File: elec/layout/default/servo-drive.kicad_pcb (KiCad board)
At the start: 4 copper layers, 37.6 x 39.9 mm, 125 parts

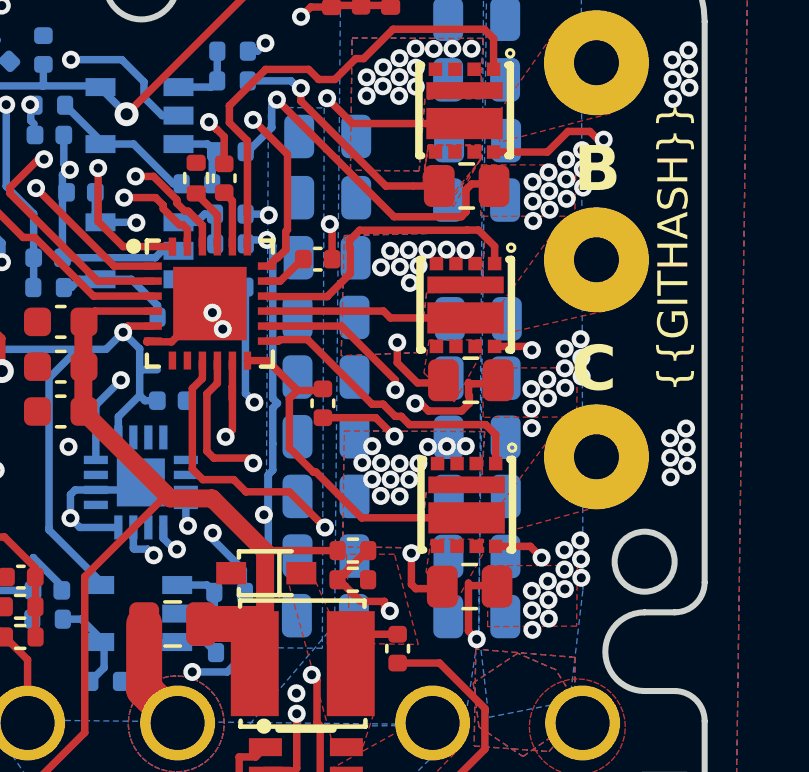
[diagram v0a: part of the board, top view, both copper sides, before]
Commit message: Flip net-ties to match improved flow
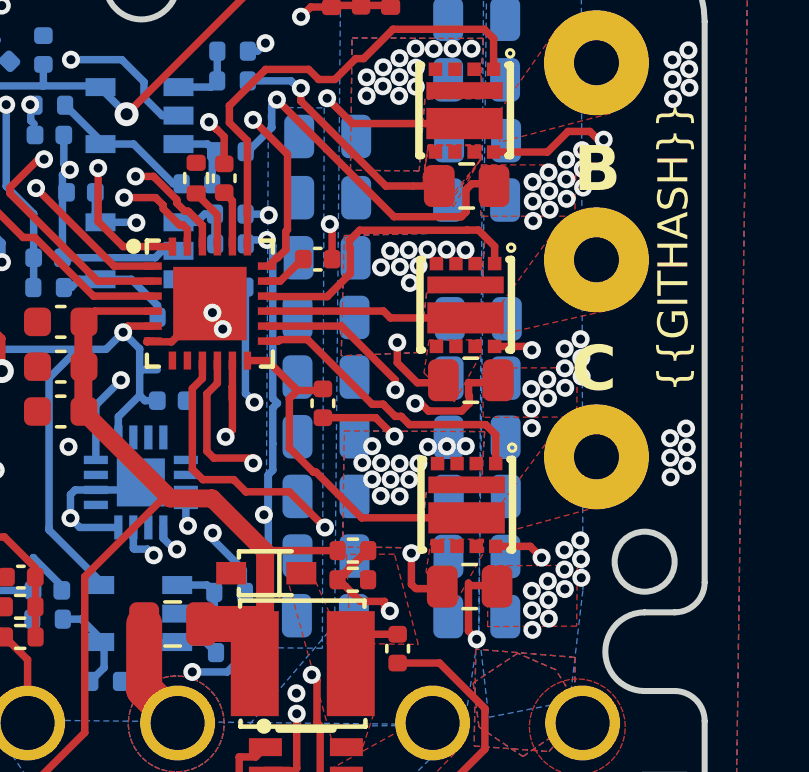
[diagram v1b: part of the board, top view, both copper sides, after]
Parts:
- C24: value 16V 220nF X7R ±10% 0402 Multilayer Ceramic Capacitors MLCC - SMD/SMT ROHS -> 16V 100nF X7R ±10% 0402 Multilayer Ceramic Capacitors MLCC - SMD/SMT ROHS
- C42, C44: value 50V 20pF C0G ±5% 0402 Multilayer Ceramic Capacitors MLCC - SMD/SMT ROHS -> 50V 18pF C0G ±5% 0402 Multilayer Ceramic Capacitors MLCC - SMD/SMT ROHS
- C9: value 50V 1uF X5R ±10% 0603 Multilayer Ceramic Capacitors MLCC - SMD/SMT ROHS -> 10V 10uF X5R ±10% 0603 Multilayer Ceramic Capacitors MLCC - SMD/SMT ROHS
- R1, R15, R20, R38: value 62.5mW Thick Film Resistors ±100ppm/℃ ±1% 10kΩ 0402 Chip Resistor - Surface Mount ROHS -> 62.5mW Thick Film Resistors 50V ±100ppm/℃ ±1% 10kΩ 0402 Chip Resistor - Surface Mount ROHS
- R10: value 62.5mW Thick Film Resistors ±100ppm/℃ ±1% 27.4kΩ 0402 Chip Resistor - Surface Mount ROHS -> 62.5mW Thick Film Resistors 50V ±100ppm/℃ ±1% 27.4kΩ 0402 Chip Resistor - Surface Mount ROHS
- R11: value 62.5mW ±1% ±200ppm/℃ 3.01kΩ 0402 Chip Resistor - Surface Mount ROHS -> 62.5mW Thick Film Resistors 50V ±100ppm/℃ ±1% 3kΩ 0402 Chip Resistor - Surface Mount ROHS
- R12, R14, R26, R45, R49, R51: value 62.5mW Thick Film Resistors ±100ppm/℃ ±1% 47kΩ 0402 Chip Resistor - Surface Mount ROHS -> 62.5mW Thick Film Resistors 50V ±100ppm/℃ ±1% 47kΩ 0402 Chip Resistor - Surface Mount ROHS
- R13, R2, R25, R44, R48, R50, R6: value 62.5mW Thick Film Resistors ±100ppm/℃ ±1% 1kΩ 0402 Chip Resistor - Surface Mount ROHS -> 62.5mW Thick Film Resistors 50V ±100ppm/℃ ±1% 1kΩ 0402 Chip Resistor - Surface Mount ROHS
- R16, R46, R52: value 62.5mW ±1% ±200ppm/℃ 73.2Ω 0402 Chip Resistor - Surface Mount ROHS -> 62.5mW Thick Film Resistors 50V -200ppm/℃~+500ppm/℃ ±1% 6.04Ω 0402 Chip Resistor - Surface Mount ROHS
- R17: value 62.5mW Thick Film Resistors ±100ppm/℃ ±1% 20.5kΩ 0402 Chip Resistor - Surface Mount ROHS -> 62.5mW Thick Film Resistors 50V ±100ppm/℃ ±1% 20.5kΩ 0402 Chip Resistor - Surface Mount ROHS
- R18: value 62.5mW Thick Film Resistors ±100ppm/℃ ±1% 6.34kΩ 0402 Chip Resistor - Surface Mount ROHS -> 62.5mW Thick Film Resistors 50V ±100ppm/℃ ±1% 6.34kΩ 0402 Chip Resistor - Surface Mount ROHS
- R19: value 10 +/- 0.1 (1%) kiloohm -> 10kohm +/- 1%
- R21: value 62.5mW Thick Film Resistors ±100ppm/℃ ±1% 11.5kΩ 0402 Chip Resistor - Surface Mount ROHS -> 62.5mW Thick Film Resistors 50V ±100ppm/℃ ±1% 11.5kΩ 0402 Chip Resistor - Surface Mount ROHS
- R22: value 62.5mW Thick Film Resistors ±100ppm/℃ ±1% 6.19kΩ 0402 Chip Resistor - Surface Mount ROHS -> 62.5mW Thick Film Resistors 50V ±100ppm/℃ ±1% 6.2kΩ 0402 Chip Resistor - Surface Mount ROHS
- R29: value 62.5mW Thick Film Resistors ±100ppm/℃ ±1% 41.2kΩ 0402 Chip Resistor - Surface Mount ROHS -> 62.5mW Thick Film Resistors 50V ±100ppm/℃ ±1% 41.2kΩ 0402 Chip Resistor - Surface Mount ROHS
- R3: value 62.5mW Thick Film Resistors ±100ppm/℃ ±1% 100kΩ 0402 Chip Resistor - Surface Mount ROHS -> 62.5mW Thick Film Resistors 50V ±100ppm/℃ ±1% 100kΩ 0402 Chip Resistor - Surface Mount ROHS
- R30: value 62.5mW Thick Film Resistors ±100ppm/℃ ±1% 4.32kΩ 0402 Chip Resistor - Surface Mount ROHS -> 62.5mW Thick Film Resistors 50V ±100ppm/℃ ±1% 4.3kΩ 0402 Chip Resistor - Surface Mount ROHS
- R31: value 62.5mW Thick Film Resistors ±100ppm/℃ ±1% 40.2kΩ 0402 Chip Resistor - Surface Mount ROHS -> 62.5mW Thick Film Resistors 50V ±100ppm/℃ ±1% 39kΩ 0402 Chip Resistor - Surface Mount ROHS
- R4, R47, R8: value (none) -> 3mΩ +/- 1%
- R5, R9: value 62.5mW Thick Film Resistors ±100ppm/℃ ±1% 5.1kΩ 0402 Chip Resistor - Surface Mount ROHS -> 62.5mW Thick Film Resistors 50V ±100ppm/℃ ±1% 5.1kΩ 0402 Chip Resistor - Surface Mount ROHS
- R7: value 62.5mW Thick Film Resistors ±100ppm/℃ ±1% 220Ω 0402 Chip Resistor - Surface Mount ROHS -> 62.5mW Thick Film Resistors 50V ±100ppm/℃ ±1% 200Ω 0402 Chip Resistor - Surface Mount ROHS
- moved U34 0.55 mm to (233.4, 103.9), turned to 180 degrees
- moved U19 0.50 mm to (235.2, 90.4), turned to 180 degrees
- moved U31 0.49 mm to (233.4, 97.0), turned to 180 degrees
- moved U17 0.49 mm to (233.3, 90.5), turned to 180 degrees
- moved U33 0.44 mm to (235.2, 97.0), turned to 180 degrees
- moved U35 0.44 mm to (235.2, 103.8), turned to 180 degrees
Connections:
- net power_stage.phase_a.half_bridge-vcc-2 renamed power_stage.phase_a.half_bridge-io
- net power_stage.phase_b.half_bridge-vcc-2 renamed power_stage.phase_b.half_bridge-io
- net power_stage.phase_c.half_bridge-vcc-2 renamed power_stage.phase_c.half_bridge-io
- R13 pad 1: power_stage.phase_a.current_sensor.bias_div-vcc -> power_stage.phase_a.current_sensor.net_tie_p-_shunt_p
- R25 pad 1: power_stage.phase_b.current_sensor.feedback_div-vcc -> power_stage.phase_b.current_sensor.net_tie_n-_shunt_n
- R3 pad 2: power_stage-gnd -> power_stage-vcc-2
- R44 pad 1: power_stage.phase_b.current_sensor.bias_div-vcc -> power_stage.phase_b.current_sensor.net_tie_p-_shunt_p
- R48 pad 1: power_stage.phase_c.current_sensor.feedback_div-vcc -> power_stage.phase_c.current_sensor.net_tie_n-_shunt_n
- R50 pad 1: power_stage.phase_c.current_sensor.bias_div-vcc -> power_stage.phase_c.current_sensor.net_tie_p-_shunt_p
- R6 pad 1: power_stage.phase_a.current_sensor.feedback_div-vcc -> power_stage.phase_a.current_sensor.net_tie_n-_shunt_n
- U17 pad 1: power_stage.phase_a.current_sensor.bias_div-vcc -> power_stage.phase_a.half_bridge-gnd
- U17 pad 2: power_stage.phase_a.half_bridge-gnd -> power_stage.phase_a.current_sensor.net_tie_p-_shunt_p
- U19 pad 1: power_stage.phase_a.current_sensor.feedback_div-vcc -> power_stage-gnd
- U19 pad 2: power_stage-gnd -> power_stage.phase_a.current_sensor.net_tie_n-_shunt_n
- U31 pad 1: power_stage.phase_b.current_sensor.bias_div-vcc -> power_stage.phase_b.half_bridge-gnd
- U31 pad 2: power_stage.phase_b.half_bridge-gnd -> power_stage.phase_b.current_sensor.net_tie_p-_shunt_p
- U33 pad 1: power_stage.phase_b.current_sensor.feedback_div-vcc -> power_stage-gnd
- U33 pad 2: power_stage-gnd -> power_stage.phase_b.current_sensor.net_tie_n-_shunt_n
- U34 pad 1: power_stage.phase_c.current_sensor.bias_div-vcc -> power_stage.phase_c.half_bridge-gnd
- U34 pad 2: power_stage.phase_c.half_bridge-gnd -> power_stage.phase_c.current_sensor.net_tie_p-_shunt_p
- U35 pad 1: power_stage.phase_c.current_sensor.feedback_div-vcc -> power_stage-gnd
- U35 pad 2: power_stage-gnd -> power_stage.phase_c.current_sensor.net_tie_n-_shunt_n
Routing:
- net power_stage.phase_c.current_sensor.net_tie_n-_shunt_n: track 0.00 -> 14.0 mm, vias 0 -> 2
- net power_stage.phase_c.current_sensor.feedback_div-vcc: track 14.0 -> 0.00 mm, vias 2 -> 0
- net power_stage.phase_b.current_sensor.net_tie_n-_shunt_n: track 0.00 -> 12.2 mm, vias 0 -> 2
- net power_stage.phase_b.current_sensor.feedback_div-vcc: track 12.2 -> 0.00 mm, vias 2 -> 0
- net power_stage.phase_a.current_sensor.net_tie_n-_shunt_n: track 0.00 -> 11.5 mm, vias 0 -> 1
- net power_stage.phase_a.current_sensor.feedback_div-vcc: track 11.5 -> 0.00 mm, vias 1 -> 0
- net power_stage.phase_c.current_sensor.net_tie_p-_shunt_p: track 0.00 -> 11.0 mm, vias 0 -> 2
- net power_stage.phase_c.current_sensor.bias_div-vcc: track 11.0 -> 0.00 mm, vias 2 -> 0
- net power_stage.phase_b.current_sensor.net_tie_p-_shunt_p: track 0.00 -> 8.98 mm, vias 0 -> 2
- net power_stage.phase_b.current_sensor.bias_div-vcc: track 8.98 -> 0.00 mm, vias 2 -> 0
- net power_stage.phase_a.current_sensor.net_tie_p-_shunt_p: track 0.00 -> 7.20 mm, vias 0 -> 1
- net power_stage.phase_a.current_sensor.bias_div-vcc: track 7.20 -> 0.00 mm, vias 1 -> 0

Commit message: Flip shunts back around to match other layouts
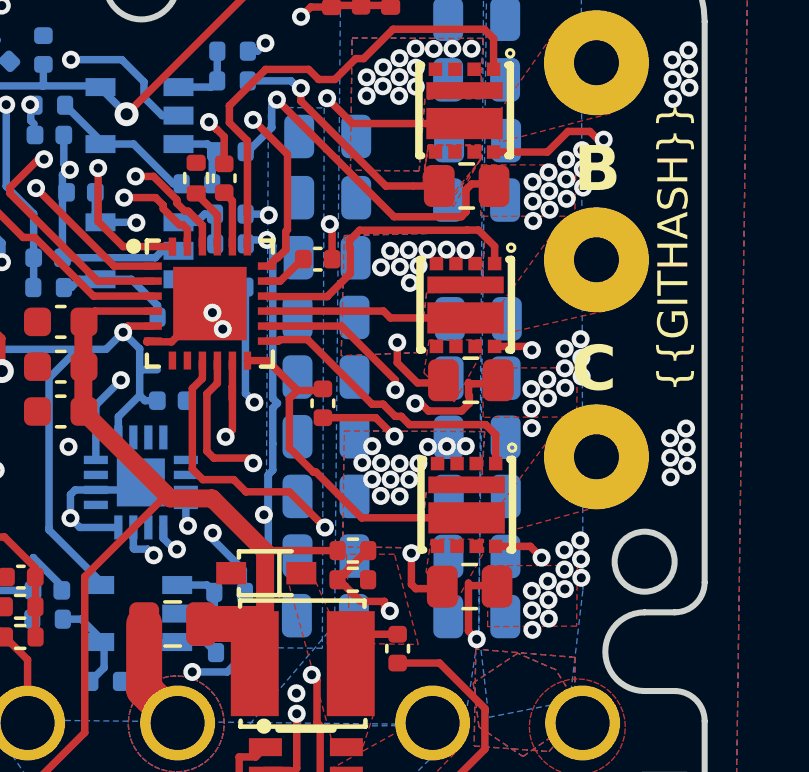
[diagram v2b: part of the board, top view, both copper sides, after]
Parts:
- C24: value 16V 100nF X7R ±10% 0402 Multilayer Ceramic Capacitors MLCC - SMD/SMT ROHS -> 16V 220nF X7R ±10% 0402 Multilayer Ceramic Capacitors MLCC - SMD/SMT ROHS
- C42, C44: value 50V 18pF C0G ±5% 0402 Multilayer Ceramic Capacitors MLCC - SMD/SMT ROHS -> 50V 20pF C0G ±5% 0402 Multilayer Ceramic Capacitors MLCC - SMD/SMT ROHS
- C9: value 10V 10uF X5R ±10% 0603 Multilayer Ceramic Capacitors MLCC - SMD/SMT ROHS -> 50V 1uF X5R ±10% 0603 Multilayer Ceramic Capacitors MLCC - SMD/SMT ROHS
- R1, R15, R20, R38: value 62.5mW Thick Film Resistors 50V ±100ppm/℃ ±1% 10kΩ 0402 Chip Resistor - Surface Mount ROHS -> 62.5mW Thick Film Resistors ±100ppm/℃ ±1% 10kΩ 0402 Chip Resistor - Surface Mount ROHS
- R10: value 62.5mW Thick Film Resistors 50V ±100ppm/℃ ±1% 27.4kΩ 0402 Chip Resistor - Surface Mount ROHS -> 62.5mW Thick Film Resistors ±100ppm/℃ ±1% 27.4kΩ 0402 Chip Resistor - Surface Mount ROHS
- R11: value 62.5mW Thick Film Resistors 50V ±100ppm/℃ ±1% 3kΩ 0402 Chip Resistor - Surface Mount ROHS -> 62.5mW ±1% ±200ppm/℃ 3.01kΩ 0402 Chip Resistor - Surface Mount ROHS
- R12, R14, R26, R45, R49, R51: value 62.5mW Thick Film Resistors 50V ±100ppm/℃ ±1% 47kΩ 0402 Chip Resistor - Surface Mount ROHS -> 62.5mW Thick Film Resistors ±100ppm/℃ ±1% 47kΩ 0402 Chip Resistor - Surface Mount ROHS
- R13, R2, R25, R44, R48, R50, R6: value 62.5mW Thick Film Resistors 50V ±100ppm/℃ ±1% 1kΩ 0402 Chip Resistor - Surface Mount ROHS -> 62.5mW Thick Film Resistors ±100ppm/℃ ±1% 1kΩ 0402 Chip Resistor - Surface Mount ROHS
- R16, R46, R52: value 62.5mW Thick Film Resistors 50V -200ppm/℃~+500ppm/℃ ±1% 6.04Ω 0402 Chip Resistor - Surface Mount ROHS -> 62.5mW ±1% ±200ppm/℃ 73.2Ω 0402 Chip Resistor - Surface Mount ROHS
- R17: value 62.5mW Thick Film Resistors 50V ±100ppm/℃ ±1% 20.5kΩ 0402 Chip Resistor - Surface Mount ROHS -> 62.5mW Thick Film Resistors ±100ppm/℃ ±1% 20.5kΩ 0402 Chip Resistor - Surface Mount ROHS
- R18: value 62.5mW Thick Film Resistors 50V ±100ppm/℃ ±1% 6.34kΩ 0402 Chip Resistor - Surface Mount ROHS -> 62.5mW Thick Film Resistors ±100ppm/℃ ±1% 6.34kΩ 0402 Chip Resistor - Surface Mount ROHS
- R19: value 10kohm +/- 1% -> 10 +/- 0.1 (1%) kiloohm
- R21: value 62.5mW Thick Film Resistors 50V ±100ppm/℃ ±1% 11.5kΩ 0402 Chip Resistor - Surface Mount ROHS -> 62.5mW Thick Film Resistors ±100ppm/℃ ±1% 11.5kΩ 0402 Chip Resistor - Surface Mount ROHS
- R22: value 62.5mW Thick Film Resistors 50V ±100ppm/℃ ±1% 6.2kΩ 0402 Chip Resistor - Surface Mount ROHS -> 62.5mW Thick Film Resistors ±100ppm/℃ ±1% 6.19kΩ 0402 Chip Resistor - Surface Mount ROHS
- R29: value 62.5mW Thick Film Resistors 50V ±100ppm/℃ ±1% 41.2kΩ 0402 Chip Resistor - Surface Mount ROHS -> 62.5mW Thick Film Resistors ±100ppm/℃ ±1% 41.2kΩ 0402 Chip Resistor - Surface Mount ROHS
- R3: value 62.5mW Thick Film Resistors 50V ±100ppm/℃ ±1% 100kΩ 0402 Chip Resistor - Surface Mount ROHS -> 62.5mW Thick Film Resistors ±100ppm/℃ ±1% 100kΩ 0402 Chip Resistor - Surface Mount ROHS
- R30: value 62.5mW Thick Film Resistors 50V ±100ppm/℃ ±1% 4.3kΩ 0402 Chip Resistor - Surface Mount ROHS -> 62.5mW Thick Film Resistors ±100ppm/℃ ±1% 4.32kΩ 0402 Chip Resistor - Surface Mount ROHS
- R31: value 62.5mW Thick Film Resistors 50V ±100ppm/℃ ±1% 39kΩ 0402 Chip Resistor - Surface Mount ROHS -> 62.5mW Thick Film Resistors ±100ppm/℃ ±1% 40.2kΩ 0402 Chip Resistor - Surface Mount ROHS
- R4, R47, R8: value 3mΩ +/- 1% -> (none)
- R5, R9: value 62.5mW Thick Film Resistors 50V ±100ppm/℃ ±1% 5.1kΩ 0402 Chip Resistor - Surface Mount ROHS -> 62.5mW Thick Film Resistors ±100ppm/℃ ±1% 5.1kΩ 0402 Chip Resistor - Surface Mount ROHS
- R7: value 62.5mW Thick Film Resistors 50V ±100ppm/℃ ±1% 200Ω 0402 Chip Resistor - Surface Mount ROHS -> 62.5mW Thick Film Resistors ±100ppm/℃ ±1% 220Ω 0402 Chip Resistor - Surface Mount ROHS
- moved U34 0.55 mm to (232.9, 103.9), turned to 0 degrees
- moved U19 0.50 mm to (234.7, 90.4), turned to 0 degrees
- moved U31 0.49 mm to (232.9, 97.0), turned to 0 degrees
- moved U17 0.49 mm to (232.8, 90.5), turned to 0 degrees
- moved U33 0.44 mm to (234.8, 97.1), turned to 0 degrees
- moved U35 0.44 mm to (234.8, 103.8), turned to 0 degrees
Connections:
- net power_stage.phase_a.half_bridge-io renamed power_stage.phase_a.half_bridge-vcc-2
- net power_stage.phase_b.half_bridge-io renamed power_stage.phase_b.half_bridge-vcc-2
- net power_stage.phase_c.half_bridge-io renamed power_stage.phase_c.half_bridge-vcc-2
- R13 pad 1: power_stage.phase_a.current_sensor.net_tie_p-_shunt_p -> power_stage.phase_a.current_sensor.bias_div-vcc
- R25 pad 1: power_stage.phase_b.current_sensor.net_tie_n-_shunt_n -> power_stage.phase_b.current_sensor.feedback_div-vcc
- R3 pad 2: power_stage-vcc-2 -> power_stage-gnd
- R44 pad 1: power_stage.phase_b.current_sensor.net_tie_p-_shunt_p -> power_stage.phase_b.current_sensor.bias_div-vcc
- R48 pad 1: power_stage.phase_c.current_sensor.net_tie_n-_shunt_n -> power_stage.phase_c.current_sensor.feedback_div-vcc
- R50 pad 1: power_stage.phase_c.current_sensor.net_tie_p-_shunt_p -> power_stage.phase_c.current_sensor.bias_div-vcc
- R6 pad 1: power_stage.phase_a.current_sensor.net_tie_n-_shunt_n -> power_stage.phase_a.current_sensor.feedback_div-vcc
- U17 pad 1: power_stage.phase_a.half_bridge-gnd -> power_stage.phase_a.current_sensor.bias_div-vcc
- U17 pad 2: power_stage.phase_a.current_sensor.net_tie_p-_shunt_p -> power_stage.phase_a.half_bridge-gnd
- U19 pad 1: power_stage-gnd -> power_stage.phase_a.current_sensor.feedback_div-vcc
- U19 pad 2: power_stage.phase_a.current_sensor.net_tie_n-_shunt_n -> power_stage-gnd
- U31 pad 1: power_stage.phase_b.half_bridge-gnd -> power_stage.phase_b.current_sensor.bias_div-vcc
- U31 pad 2: power_stage.phase_b.current_sensor.net_tie_p-_shunt_p -> power_stage.phase_b.half_bridge-gnd
- U33 pad 1: power_stage-gnd -> power_stage.phase_b.current_sensor.feedback_div-vcc
- U33 pad 2: power_stage.phase_b.current_sensor.net_tie_n-_shunt_n -> power_stage-gnd
- U34 pad 1: power_stage.phase_c.half_bridge-gnd -> power_stage.phase_c.current_sensor.bias_div-vcc
- U34 pad 2: power_stage.phase_c.current_sensor.net_tie_p-_shunt_p -> power_stage.phase_c.half_bridge-gnd
- U35 pad 1: power_stage-gnd -> power_stage.phase_c.current_sensor.feedback_div-vcc
- U35 pad 2: power_stage.phase_c.current_sensor.net_tie_n-_shunt_n -> power_stage-gnd
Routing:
- net power_stage.phase_c.current_sensor.net_tie_n-_shunt_n: track 14.0 -> 0.00 mm, vias 2 -> 0
- net power_stage.phase_c.current_sensor.feedback_div-vcc: track 0.00 -> 14.0 mm, vias 0 -> 2
- net power_stage.phase_b.current_sensor.net_tie_n-_shunt_n: track 12.2 -> 0.00 mm, vias 2 -> 0
- net power_stage.phase_b.current_sensor.feedback_div-vcc: track 0.00 -> 12.2 mm, vias 0 -> 2
- net power_stage.phase_a.current_sensor.net_tie_n-_shunt_n: track 11.5 -> 0.00 mm, vias 1 -> 0
- net power_stage.phase_a.current_sensor.feedback_div-vcc: track 0.00 -> 11.5 mm, vias 0 -> 1
- net power_stage.phase_c.current_sensor.net_tie_p-_shunt_p: track 11.0 -> 0.00 mm, vias 2 -> 0
- net power_stage.phase_c.current_sensor.bias_div-vcc: track 0.00 -> 11.0 mm, vias 0 -> 2
- net power_stage.phase_b.current_sensor.net_tie_p-_shunt_p: track 8.98 -> 0.00 mm, vias 2 -> 0
- net power_stage.phase_b.current_sensor.bias_div-vcc: track 0.00 -> 8.98 mm, vias 0 -> 2
- net power_stage.phase_a.current_sensor.net_tie_p-_shunt_p: track 7.20 -> 0.00 mm, vias 1 -> 0
- net power_stage.phase_a.current_sensor.bias_div-vcc: track 0.00 -> 7.20 mm, vias 0 -> 1
